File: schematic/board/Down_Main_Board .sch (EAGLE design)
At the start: 19 parts, among them J1 MCX-J-P-H-ST-TH1, J2 U.FL-R-SMT-1_10_

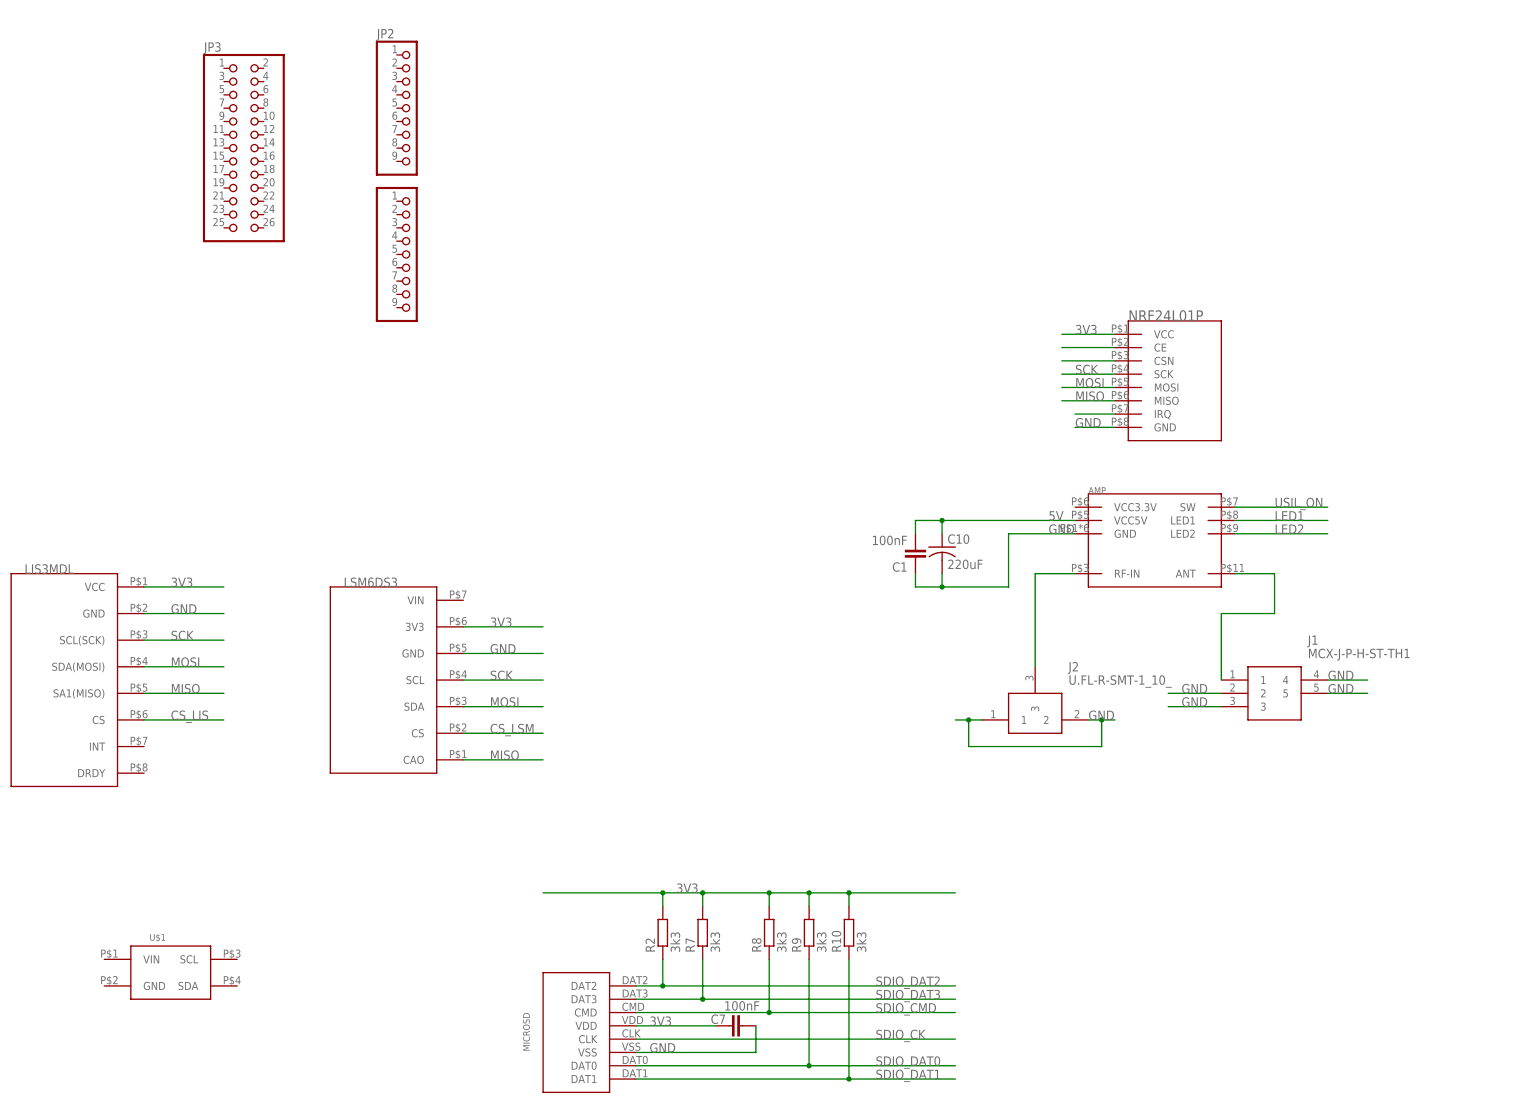
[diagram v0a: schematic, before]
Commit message: 100501 раз изменил пины на плате
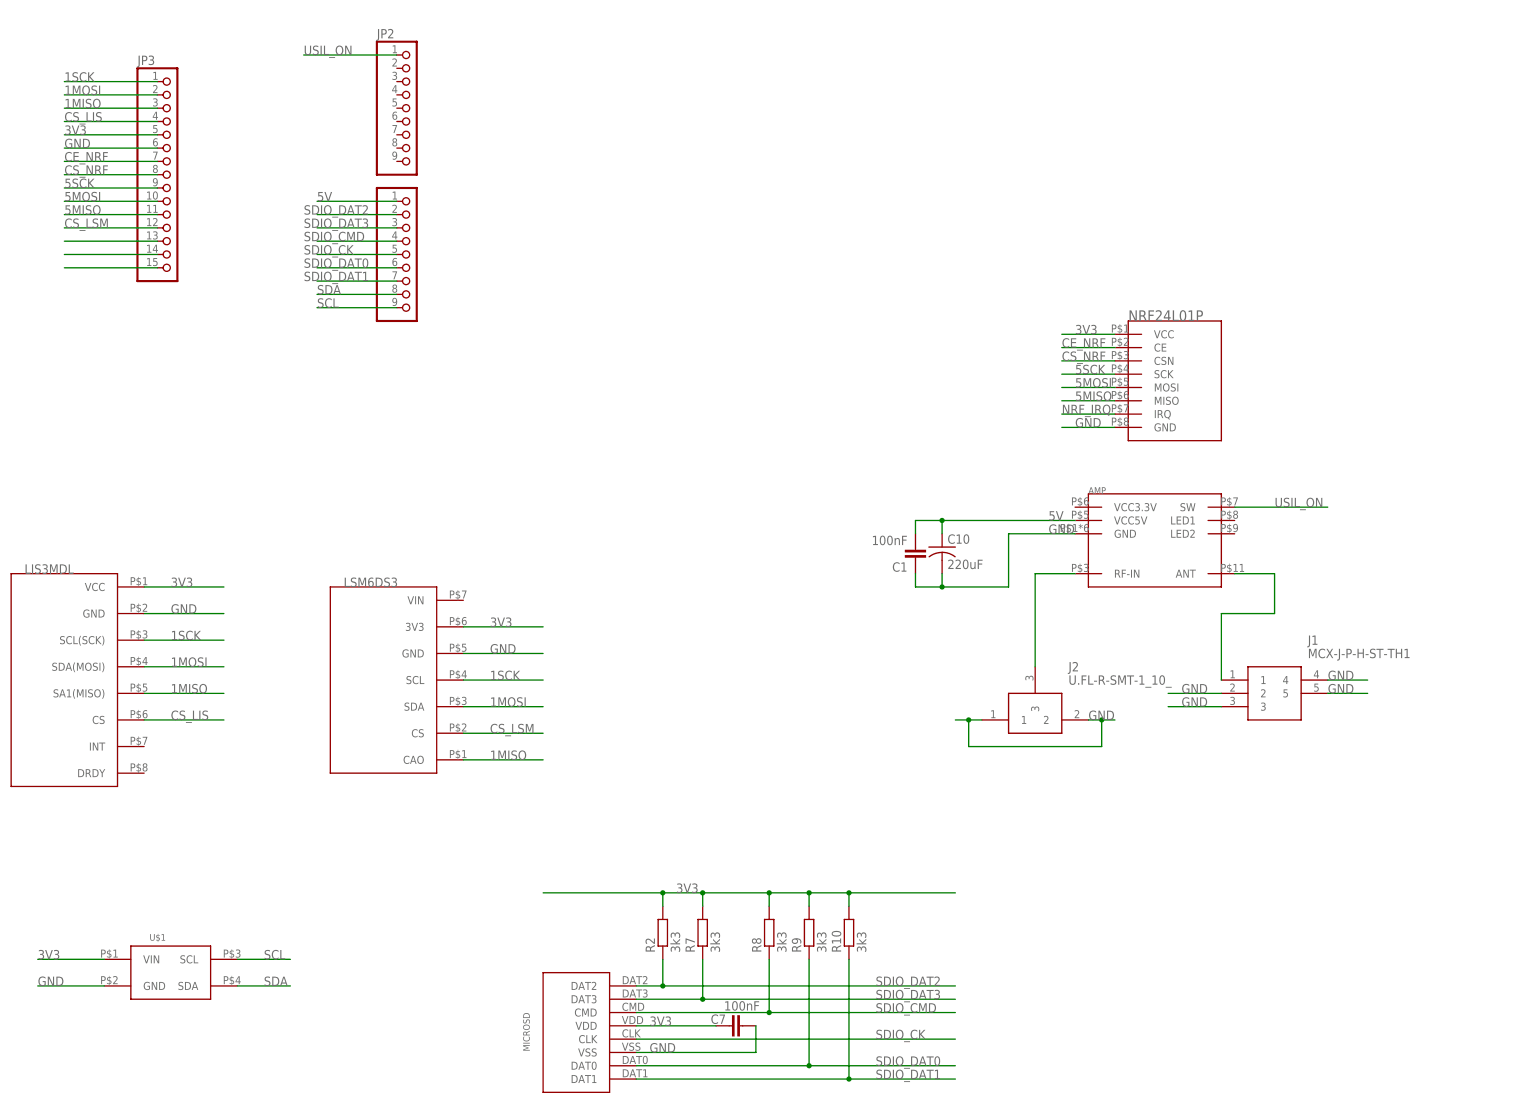
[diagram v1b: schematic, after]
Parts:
- JP3: device pinhead:PINHD-2X13 -> pinhead:PINHD-1X15
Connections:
- removed net LED1: AMP.LED1
- removed net LED2: AMP.LED2
- removed net MISO: LIS3MDL.SA1(MISO), LSM6DS3.CAO, NRF24L01P.MISO
- removed net MOSI: LIS3MDL.SDA(MOSI), LSM6DS3.SDA, NRF24L01P.MOSI
- removed net SCK: LIS3MDL.SCL(SCK), LSM6DS3.SCL, NRF24L01P.SCK
- new net 1MISO: JP3.3, LIS3MDL.SA1(MISO), LSM6DS3.CAO
- new net 1MOSI: JP3.2, LIS3MDL.SDA(MOSI), LSM6DS3.SDA
- new net 1SCK: JP3.1, LIS3MDL.SCL(SCK), LSM6DS3.SCL
- new net 5MISO: JP3.11, NRF24L01P.MISO
- new net 5MOSI: JP3.10, NRF24L01P.MOSI
- new net 5SCK: JP3.9, NRF24L01P.SCK
- new net N$11: JP3.13
- new net N$12: JP3.14
- new net N$13: JP3.15
- new net SCL: JP1.9, U$1.SCL
- new net SDA: JP1.8, U$1.SDA
- net 3V3: now also JP3.5, U$1.VIN
- net 5V: now also JP1.1
- net CE_NRF: now also JP3.7
- net CS_LIS: now also JP3.4
- net CS_LSM: now also JP3.12
- net CS_NRF: now also JP3.8
- net GND: now also JP3.6, U$1.GND
- net SDIO_CK: now also JP1.5
- net SDIO_CMD: now also JP1.4
- net SDIO_DAT0: now also JP1.6
- net SDIO_DAT1: now also JP1.7
- net SDIO_DAT2: now also JP1.2
- net SDIO_DAT3: now also JP1.3
- net USIL_ON: now also JP2.1

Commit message: почти добавил новый разъём
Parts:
- added BUZZER: BUZZERS8R6, NEON-BLADE-2023:BUZZERS8R6
- added R30: 100R, rcl:R-EU_R0603
- added R31: 10k, rcl:R-EU_R0603
- added SI2301: MOSFET-N, NEON-BLADE-2023:MOSFET-N
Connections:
- removed net N$11: JP3.13
- new net BUZZER: JP3.13, R30.1
- new net N$1: R30.2, R31.1, SI2301.G
- new net N$20: BUZZER.GND, SI2301.D
- net 5V: now also BUZZER.VIN
- net GND: now also R31.2, SI2301.S
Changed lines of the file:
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@@
 <part name="U$1" library="NEON-BLADE-2024" deviceset="BME280" device="BME280-PINS-ONLY"/>
 <part name="JP3" library="pinhead" library_urn="urn:adsk.eagle:library:325" deviceset="PINHD-1X15" device="" package3d_urn="urn:adsk.eagle:package:22424/2"/>
+<part name="BUZZER" library="NEON-BLADE-2023" deviceset="BUZZER" device="S8R6"/>
+<part name="SI2301" library="NEON-BLADE-2023" deviceset="MOSFET-N" device=""/>
+<part name="R30" library="rcl" library_urn="urn:adsk.eagle:library:334" deviceset="R-EU_" device="R0603" package3d_urn="urn:adsk.eagle:package:23555/3" value="100R"/>
+<part name="R31" library="rcl" library_urn="urn:adsk.eagle:library:334" deviceset="R-EU_" device="R0603" package3d_urn="urn:adsk.eagle:package:23555/3" value="10k"/>
 </parts>
 <sheets>
@@
 <attribute name="NAME" x="41.91" y="280.035" size="1.778" layer="95"/>
 <attribute name="VALUE" x="41.91" y="236.22" size="1.778" layer="96"/>
+</instance>
+<instance part="BUZZER" gate="G$1" x="233.68" y="254" smashed="yes" rot="R180">
+<attribute name="NAME" x="241.3" y="248.92" size="2.54" layer="95" rot="R180"/>
+</instance>
+<instance part="SI2301" gate="G$1" x="213.36" y="256.54" smashed="yes" rot="R270">
+<attribute name="NAME" x="213.995" y="251.46" size="1.27" layer="95" rot="R270"/>
+<attribute name="VALUE" x="212.09" y="251.46" size="1.27" layer="96" rot="R270"/>
+</instance>
+<instance part="R30" gate="G$1" x="195.58" y="274.32" smashed="yes">
+<attribute name="NAME" x="191.77" y="275.8186" size="1.778" layer="95"/>
+<attribute name="VALUE" x="191.77" y="271.018" size="1.778" layer="96"/>
+</instance>
+<instance part="R31" gate="G$1" x="203.2" y="264.16" smashed="yes" rot="R270">
+<attribute name="NAME" x="204.6986" y="267.97" size="1.778" layer="95" rot="R270"/>
+<attribute name="VALUE" x="199.898" y="267.97" size="1.778" layer="96" rot="R270"/>
 </instance>
 </instances>
@@
 <wire x1="45.72" y1="264.16" x2="27.94" y2="264.16" width="0.1524" layer="91"/>
 <label x="27.94" y="264.16" size="1.778" layer="95"/>
+</segment>
+<segment>
+<pinref part="R31" gate="G$1" pin="2"/>
+<pinref part="SI2301" gate="G$1" pin="S"/>
+<wire x1="203.2" y1="259.08" x2="203.2" y2="254" width="0.1524" layer="91"/>
+<wire x1="203.2" y1="254" x2="208.28" y2="254" width="0.1524" layer="91"/>
+<wire x1="203.2" y1="254" x2="182.88" y2="254" width="0.1524" layer="91"/>
+<junction x="203.2" y="254"/>
+<label x="182.88" y="254" size="1.778" layer="95"/>
 </segment>
 </net>
@@
 <label x="76.2" y="254" size="1.778" layer="95"/>
 </segment>
+<segment>
+<pinref part="BUZZER" gate="G$1" pin="VIN"/>
+<wire x1="246.38" y1="254" x2="254" y2="254" width="0.1524" layer="91"/>
+<label x="251.46" y="254" size="1.778" layer="95"/>
+</segment>
 </net>
 <net name="USIL_ON" class="0">
@@
 </segment>
 </net>
-<net name="N$11" class="0">
+<net name="BUZZER" class="0">
 <segment>
 <pinref part="JP3" gate="A" pin="13"/>
 <wire x1="45.72" y1="246.38" x2="27.94" y2="246.38" width="0.1524" layer="91"/>
+<label x="27.94" y="246.38" size="1.778" layer="95"/>
+</segment>
+<segment>
+<pinref part="R30" gate="G$1" pin="1"/>
+<wire x1="190.5" y1="274.32" x2="180.34" y2="274.32" width="0.1524" layer="91"/>
+<label x="172.72" y="274.32" size="1.778" layer="95"/>
 </segment>
 </net>
@@
 </segment>
 </net>
+<net name="N$20" class="0">
+<segment>
+<pinref part="BUZZER" gate="G$1" pin="GND"/>
+<pinref part="SI2301" gate="G$1" pin="D"/>
+<wire x1="218.44" y1="254" x2="220.98" y2="254" width="0.1524" layer="91"/>
+</segment>
+</net>
+<net name="N$1" class="0">
+<segment>
+<pinref part="R30" gate="G$1" pin="2"/>
+<pinref part="SI2301" gate="G$1" pin="G"/>
+<wire x1="200.66" y1="274.32" x2="203.2" y2="274.32" width="0.1524" layer="91"/>
+<wire x1="203.2" y1="274.32" x2="210.82" y2="274.32" width="0.1524" layer="91"/>
+<wire x1="210.82" y1="274.32" x2="210.82" y2="259.08" width="0.1524" layer="91"/>
+<pinref part="R31" gate="G$1" pin="1"/>
+<wire x1="203.2" y1="269.24" x2="203.2" y2="274.32" width="0.1524" layer="91"/>
+<junction x="203.2" y="274.32"/>
+</segment>
+</net>

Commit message: переделки по плате
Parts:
- removed JP1, JP2: (no value), pinhead:PINHD-1X9
- removed JP3: (no value), pinhead:PINHD-1X15
- added U$2, U$3, U$6, U$7: PBS_SMD_X9, NEON-BLADE-2024:PBS_SMD_X9
- added U$4, U$8: PBS_SMD_X15, NEON-BLADE-2024:PBS_SMD_X15
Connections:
- new net N$2: U$4.14
- new net N$3: U$4.15
- net 1MISO: now also U$4.3, U$8.3; no longer JP3.3
- net 1MOSI: now also U$4.2, U$8.2; no longer JP3.2
- net 1SCK: now also U$4.1, U$8.1; no longer JP3.1
- net 3V3: now also U$4.5, U$8.5; no longer JP3.5
- net 5MISO: now also U$4.11, U$8.11; no longer JP3.11
- net 5MOSI: now also U$4.10, U$8.10; no longer JP3.10
- net 5SCK: now also U$4.9, U$8.9; no longer JP3.9
- net 5V: now also U$2.1, U$6.1; no longer JP1.1
- net BUZZER: now also U$4.13, U$8.13; no longer JP3.13
- net CE_NRF: now also U$4.7, U$8.7; no longer JP3.7
- net CS_LIS: now also U$4.4, U$8.4; no longer JP3.4
- net CS_LSM: now also U$4.12, U$8.12; no longer JP3.12
- net CS_NRF: now also U$4.8, U$8.8; no longer JP3.8
- net GND: now also U$4.6, U$8.6; no longer JP3.6
- net N$12: now also U$8.14; no longer JP3.14
- net N$13: now also U$8.15; no longer JP3.15
- net SCL: now also U$2.9, U$6.9; no longer JP1.9
- net SDA: now also U$2.8, U$6.8; no longer JP1.8
- net SDIO_CK: now also U$2.5, U$6.5; no longer JP1.5
- net SDIO_CMD: now also U$2.4, U$6.4; no longer JP1.4
- net SDIO_DAT0: now also U$2.6, U$6.6; no longer JP1.6
- net SDIO_DAT1: now also U$2.7, U$6.7; no longer JP1.7
- net SDIO_DAT2: now also U$2.2, U$6.2; no longer JP1.2
- net SDIO_DAT3: now also U$2.3, U$6.3; no longer JP1.3
- net USIL_ON: now also U$3.1, U$7.1; no longer JP2.1

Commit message: Почти доделал нижнюю плату
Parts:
- added LED1, LED2: (no value), led:LEDCHIPLED_0603
- added R1, R3: 100R, rcl:R-EU_R0603
- added U$5, U$9: VIAS-SELECT, NEON-BLADE-2024:VIAS-SELECT
- LIS3MDL: value LIS3MDL-CJMCUБез_отв._зеркальный -> LIS3MDL-CJMCUбез_отв.; device NEON-BLADE-2023:LIS3MDL-CJMCUБез_отв._зеркальный -> NEON-BLADE-2023:LIS3MDL-CJMCUбез_отв.
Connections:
- new net N$10: U$3.6, U$7.6
- new net N$11: U$3.7, U$7.7
- new net N$14: U$3.8, U$7.8
- new net N$15: U$3.9, U$7.9
- new net N$16: LED1.C, U$5.TOP
- new net N$17: LED1.A, R1.2
- new net N$18: AMP.LED1, R1.1
- new net N$19: LED2.C, U$9.TOP
- new net N$21: LED2.A, R3.2
- new net N$22: AMP.LED2, R3.1
- new net N$6: U$3.2, U$7.2
- new net N$7: U$3.3, U$7.3
- new net N$8: U$3.4, U$7.4
- new net N$9: U$3.5, U$7.5
- net 5V: now also U$5.RIGHT, U$9.RIGHT
- net GND: now also U$5.LEFT, U$9.LEFT
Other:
- moved on the sheet: U$4, U$6, U$7, U$8

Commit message: Проверил плату нижнюю
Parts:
- added U$10: VIAS-SELECT, NEON-BLADE-2024:VIAS-SELECT
- renumbered AMP to AMPLIFIRE
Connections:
- removed net N$13: U$8.15
- net 1MISO: now also U$8.13; no longer U$8.3
- net 1MOSI: now also U$8.14; no longer U$8.2
- net 1SCK: now also U$8.15; no longer U$8.1
- net 3V3: now also U$8.11; no longer U$8.5
- net 5MISO: now also U$8.5; no longer U$8.11
- net 5MOSI: now also U$8.6; no longer U$8.10
- net 5SCK: now also U$8.7; no longer U$8.9
- net 5V: now also U$10.RIGHT, U$2.9; no longer U$2.1
- net BUZZER: now also U$8.3; no longer U$8.13
- net CE_NRF: now also U$8.9; no longer U$8.7
- net CS_LIS: now also U$8.12; no longer U$8.4
- net CS_LSM: now also U$8.4; no longer U$8.12
- net GND: now also U$10.LEFT, U$8.10; no longer U$8.6
- net N$10: now also U$3.4; no longer U$3.6
- net N$11: now also U$3.3; no longer U$3.7
- net N$12: now also U$3.9, U$7.1; no longer U$8.14
- net N$14: now also U$3.2; no longer U$3.8
- net N$15: now also U$3.1; no longer U$3.9
- net N$2: now also U$8.2
- net N$3: now also U$8.1
- net N$6: now also U$3.8; no longer U$3.2
- net N$7: now also U$3.7; no longer U$3.3
- net N$8: now also U$3.6; no longer U$3.4
- net SCL: now also U$2.1; no longer U$2.9
- net SDA: now also U$2.2; no longer U$2.8
- net SDIO_CMD: now also U$2.6; no longer U$2.4
- net SDIO_DAT0: now also U$2.4; no longer U$2.6
- net SDIO_DAT1: now also U$2.3; no longer U$2.7
- net SDIO_DAT2: now also U$2.8; no longer U$2.2
- net SDIO_DAT3: now also U$2.7; no longer U$2.3
- net USIL_ON: now also U$10.TOP; no longer U$3.1, U$7.1
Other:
- moved on the sheet: U$2, U$3, U$7, U$8

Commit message: Внес поправки
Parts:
- R1, R3: value 100R -> 2k
- renumbered J1 to RADIO, J2 to ANT
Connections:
- removed net NRF_IRQ: NRF24L01P.IRQ
- net 3V3: no longer U$1.VIN
- net 5V: now also U$1.VIN
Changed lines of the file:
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@@
 <part name="R10" library="rcl" library_urn="urn:adsk.eagle:library:334" deviceset="R-EU_" device="R0603" package3d_urn="urn:adsk.eagle:package:23555/3" value="3k3"/>
 <part name="AMPLIFIRE" library="NEON-BLADE-2023" deviceset="XQ-02A" device=""/>
-<part name="J1" library="MCX-J-P-H-ST-TH1" deviceset="MCX-J-P-H-ST-TH1" device=""/>
-<part name="J2" library="U.FL-R-SMT-1_10_" deviceset="U.FL-R-SMT-1_10_" device=""/>
+<part name="RADIO" library="MCX-J-P-H-ST-TH1" deviceset="MCX-J-P-H-ST-TH1" device=""/>
+<part name="ANT" library="U.FL-R-SMT-1_10_" deviceset="U.FL-R-SMT-1_10_" device=""/>
 <part name="C1" library="rcl" library_urn="urn:adsk.eagle:library:334" deviceset="C-EU" device="C0603" package3d_urn="urn:adsk.eagle:package:23616/2" value="100nF"/>
 <part name="C10" library="NEON-BLADE-2023" deviceset="ECAP" device="ECAP220" value="220uF"/>
@@
 <part name="LED1" library="led" library_urn="urn:adsk.eagle:library:259" deviceset="LED" device="CHIPLED_0603" package3d_urn="urn:adsk.eagle:package:15822/2"/>
 <part name="U$5" library="NEON-BLADE-2024" deviceset="VIAS-SELECT" device=""/>
-<part name="R1" library="rcl" library_urn="urn:adsk.eagle:library:334" deviceset="R-EU_" device="R0603" package3d_urn="urn:adsk.eagle:package:23555/3" value="100R"/>
+<part name="R1" library="rcl" library_urn="urn:adsk.eagle:library:334" deviceset="R-EU_" device="R0603" package3d_urn="urn:adsk.eagle:package:23555/3" value="2k"/>
 <part name="LED2" library="led" library_urn="urn:adsk.eagle:library:259" deviceset="LED" device="CHIPLED_0603" package3d_urn="urn:adsk.eagle:package:15822/2"/>
 <part name="U$9" library="NEON-BLADE-2024" deviceset="VIAS-SELECT" device=""/>
-<part name="R3" library="rcl" library_urn="urn:adsk.eagle:library:334" deviceset="R-EU_" device="R0603" package3d_urn="urn:adsk.eagle:package:23555/3" value="100R"/>
+<part name="R3" library="rcl" library_urn="urn:adsk.eagle:library:334" deviceset="R-EU_" device="R0603" package3d_urn="urn:adsk.eagle:package:23555/3" value="2k"/>
 <part name="U$8" library="NEON-BLADE-2024" deviceset="PBS_SMD_X15" device=""/>
 <part name="U$3" library="NEON-BLADE-2024" deviceset="PBS_SMD_X9" device=""/>
@@
 <attribute name="NAME" x="223.52" y="198.12" size="1.27" layer="95"/>
 </instance>
-<instance part="J1" gate="G$1" x="248.92" y="162.56" smashed="yes">
+<instance part="RADIO" gate="G$1" x="248.92" y="162.56" smashed="yes">
 <attribute name="NAME" x="265.43" y="170.18" size="1.778" layer="95" align="center-left"/>
 <attribute name="VALUE" x="265.43" y="167.64" size="1.778" layer="96" align="center-left"/>
 </instance>
-<instance part="J2" gate="G$1" x="203.2" y="154.94" smashed="yes">
+<instance part="ANT" gate="G$1" x="203.2" y="154.94" smashed="yes">
 <attribute name="NAME" x="219.71" y="165.1" size="1.778" layer="95" align="center-left"/>
 <attribute name="VALUE" x="219.71" y="162.56" size="1.778" layer="96" align="center-left"/>
@@
 </segment>
 <segment>
-<pinref part="J1" gate="G$1" pin="2"/>
+<pinref part="RADIO" gate="G$1" pin="2"/>
 <wire x1="248.92" y1="160.02" x2="238.76" y2="160.02" width="0.1524" layer="91"/>
 <label x="241.3" y="160.02" size="1.778" layer="95"/>
 </segment>
 <segment>
-<pinref part="J1" gate="G$1" pin="3"/>
+<pinref part="RADIO" gate="G$1" pin="3"/>
 <wire x1="248.92" y1="157.48" x2="238.76" y2="157.48" width="0.1524" layer="91"/>
 <label x="241.3" y="157.48" size="1.778" layer="95"/>
 </segment>
 <segment>
-<pinref part="J1" gate="G$1" pin="4"/>
+<pinref part="RADIO" gate="G$1" pin="4"/>
 <wire x1="269.24" y1="162.56" x2="276.86" y2="162.56" width="0.1524" layer="91"/>
 <label x="269.24" y="162.56" size="1.778" layer="95"/>
 </segment>
 <segment>
-<pinref part="J1" gate="G$1" pin="5"/>
+<pinref part="RADIO" gate="G$1" pin="5"/>
 <wire x1="269.24" y1="160.02" x2="276.86" y2="160.02" width="0.1524" layer="91"/>
 <label x="269.24" y="160.02" size="1.778" layer="95"/>
 </segment>
 <segment>
-<pinref part="J2" gate="G$1" pin="2"/>
+<pinref part="ANT" gate="G$1" pin="2"/>
 <wire x1="223.52" y1="154.94" x2="226.06" y2="154.94" width="0.1524" layer="91"/>
 <label x="223.52" y="154.94" size="1.778" layer="95"/>
-<pinref part="J2" gate="G$1" pin="1"/>
+<pinref part="ANT" gate="G$1" pin="1"/>
 <wire x1="226.06" y1="154.94" x2="228.6" y2="154.94" width="0.1524" layer="91"/>
 <wire x1="203.2" y1="154.94" x2="200.66" y2="154.94" width="0.1524" layer="91"/>
@@
 </segment>
 <segment>
-<pinref part="U$1" gate="G$1" pin="VIN"/>
-<wire x1="35.56" y1="109.22" x2="22.86" y2="109.22" width="0.1524" layer="91"/>
-<label x="22.86" y="109.22" size="1.778" layer="95"/>
-</segment>
-<segment>
 <wire x1="76.2" y1="266.7" x2="50.8" y2="266.7" width="0.1524" layer="91"/>
 <label x="58.42" y="266.7" size="1.778" layer="95"/>
@@
 <label x="302.26" y="238.76" size="1.778" layer="95" rot="R90"/>
 </segment>
+<segment>
+<pinref part="U$1" gate="G$1" pin="VIN"/>
+<wire x1="35.56" y1="109.22" x2="22.86" y2="109.22" width="0.1524" layer="91"/>
+<label x="22.86" y="109.22" size="1.778" layer="95"/>
+</segment>
 </net>
 <net name="USIL_ON" class="0">
@@
 <net name="N$4" class="0">
 <segment>
-<pinref part="J2" gate="G$1" pin="3"/>
+<pinref part="ANT" gate="G$1" pin="3"/>
 <pinref part="AMPLIFIRE" gate="G$1" pin="RF-IN"/>
 <wire x1="213.36" y1="165.1" x2="213.36" y2="182.88" width="0.1524" layer="91"/>
@@
 <net name="N$5" class="0">
 <segment>
-<pinref part="J1" gate="G$1" pin="1"/>
+<pinref part="RADIO" gate="G$1" pin="1"/>
 <wire x1="248.92" y1="162.56" x2="248.92" y2="175.26" width="0.1524" layer="91"/>
 <wire x1="248.92" y1="175.26" x2="259.08" y2="175.26" width="0.1524" layer="91"/>
@@
 </segment>
 </net>
-<net name="NRF_IRQ" class="0">
-<segment>
-<pinref part="NRF24L01P" gate="G$1" pin="IRQ"/>
-<wire x1="228.6" y1="213.36" x2="218.44" y2="213.36" width="0.1524" layer="91"/>
-<label x="218.44" y="213.36" size="1.778" layer="95"/>
-</segment>
-</net>
